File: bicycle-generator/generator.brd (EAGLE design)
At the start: 100 x 80 mm, 61 parts, among them IC1 MC34063AD, K1 ARK500/2, K2 ARK500/2, K3 ARK500/2, K4 ARK500/2, K5 ARK500/2, K6 HEAT_NPN, K7 ARK500/2, K8 ARK500/2, Q1 IRF3704S, Q4 IRFR5305, T1 BC807, T2 BC807, X1 CV_LED, X2 PWR_LED, X3 5V_SW, X4 5V_LED, X5 5V_OUT

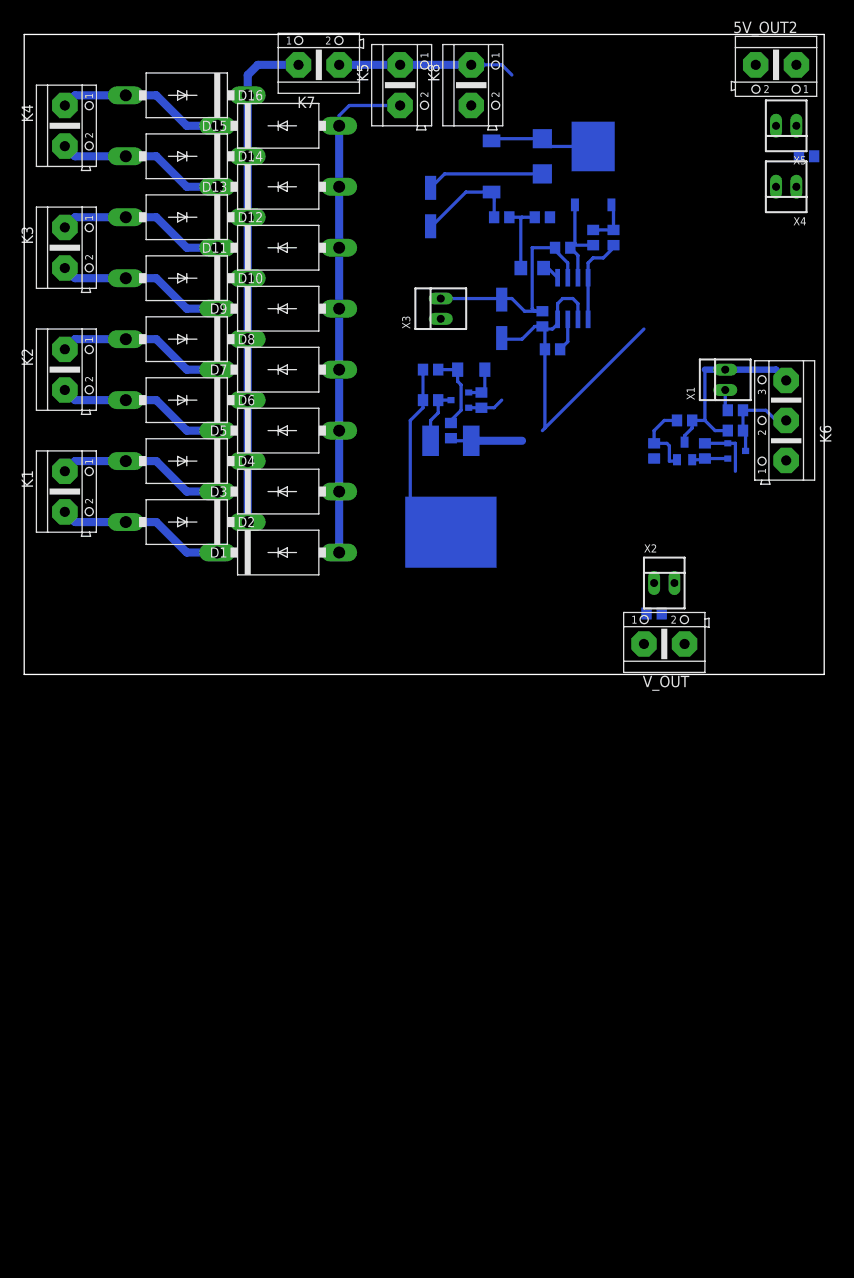
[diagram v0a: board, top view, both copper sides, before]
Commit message: Use N-channel MOSFET with pulldown.
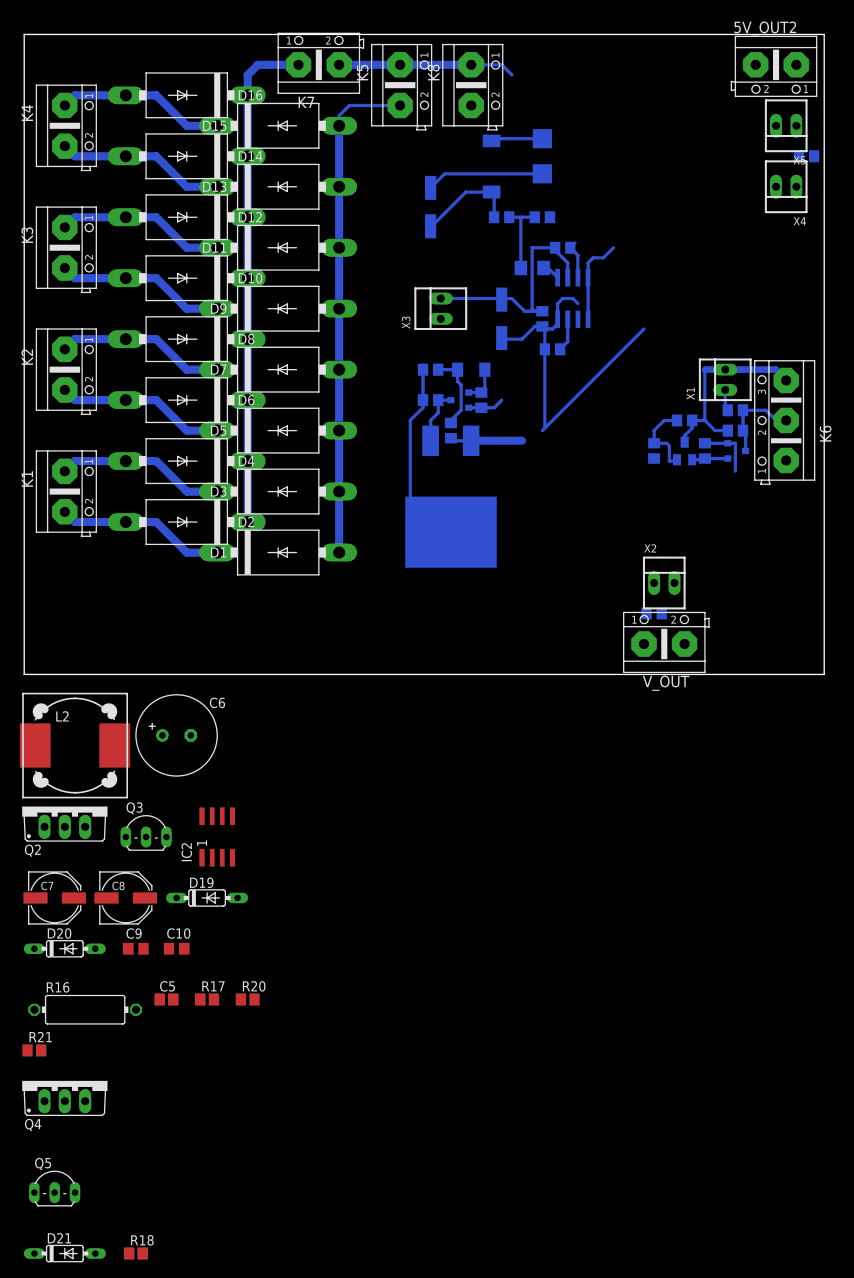
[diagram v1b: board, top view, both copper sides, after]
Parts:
- removed R19: 330, rcl:R0805
- added C10: 10n, rcl:C0805
- added C5: 680p, resistor:C0805
- added C6: 10uF, 200V, resistor:E3,5-10
- added C7, C8: 100uF, resistor:PANASONIC_D
- added C9: 100n, rcl:C0805
- added D19: BAV21, diode:DO35-7
- added D20, D21: 1N914, diode:DO35-7
- added IC2: MC34063SO, #Krakonos:SOP08
- added L2: DR127, 330uH, inductors:DR127
- added Q2: IRF740, transistor-power:TO220BV
- added Q3, Q5: MPSA56, transistor-pnp:TO92-CBE
- added R16: R1, 2W, resistor:V234/12
- added R17, R21: 1k, resistor:R0805
- added R20: 150k, 200V, resistor:R0805
- Q4: value IRFR5305 -> IRF740; device transistor-power:D-PAK_TO252AA -> transistor-power:TO220BV
- R18: value 820 -> 1k; device rcl:R0805 -> resistor:R0805
- moved R18 140.3 mm to (14.0, -72.4), flipped to the top, turned to 0 degrees
- moved Q4 132.0 mm to (5.08, -50.8), flipped to the top
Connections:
- new net 200V: C6.+, D19.C, R20.1
- new net N$25: C10.1, IC2.5, R17.2, R20.2
- new net N$26: C5.1, IC2.3
- new net N$29: D19.A, L2.2, Q2.D
- new net N$30: D20.C, Q2.G, Q3.E
- new net N$31: D20.A, IC2.2, Q3.B, R21.1
- new net N$32: C8.+, IC2.1, IC2.7, IC2.8, L2.1, R16.2
- new net N$33: D21.A, IC1.2
- new net VCC: C7.+, C9.1, IC2.6, R16.1
- net GND: now also C10.2, C5.2, C6.-, C7.-, C8.-, C9.2, IC2.4, Q2.S, Q3.C, Q5.C, R17.1, R18.2, R21.2; no longer IC1.2
- net N$15: now also D21.C, Q4.G, Q5.E; no longer IC1.1, IC1.8, R18.2
- net N$19: now also Q4.S; no longer Q4.4
- net N$27: now also IC1.1, IC1.7, IC1.8, Q4.D, R13.2; no longer Q4.1, R18.1, R19.2
- net N$28: now also Q5.B, R18.1; no longer IC1.7, Q4.3, R13.2, R19.1
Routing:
- net N$28: track 12.7 -> 0.00 mm
- net N$15: track 11.3 -> 0.00 mm
- net N$27: track 5.79 -> 16.4 mm
- net N$19: track 13.2 -> 7.83 mm
- net GND: track 69.7 -> 67.8 mm

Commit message: First version routed.
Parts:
- removed C10: 10n, rcl:C0805
- removed C5: 680p, resistor:C0805
- removed C6: 10uF, 200V, resistor:E3,5-10
- removed C7, C8: 100uF, resistor:PANASONIC_D
- removed C9: 100n, rcl:C0805
- removed D20, D21: 1N914, diode:DO35-7
- removed IC2: MC34063SO, #Krakonos:SOP08
- removed L2: DR127, 330uH, inductors:DR127
- removed Q3, Q5: MPSA56, transistor-pnp:TO92-CBE
- removed Q4: IRF740, transistor-power:TO220BV
- removed R16: R1, 2W, resistor:V234/12
- removed R17, R21: 1k, resistor:R0805
- removed R20: 150k, 200V, resistor:R0805
- added T3: (no value), transistor:SOT23-BEC
- D19: value BAV21 -> LL4148-MINIMELF; device diode:DO35-7 -> diode:SOD80C
- Q2: value IRF740 -> IRF3704S; device transistor-power:TO220BV -> transistor-power:D2PACK
- moved R18 114.8 mm to (62.2, 31.8), flipped to the bottom, turned to 90 degrees
- moved D19 66.9 mm to (59.7, 27.9), flipped to the bottom, turned to 180 degrees
- moved Q2 65.4 mm to (62.2, 15.2), flipped to the bottom, turned to 180 degrees
- moved C3 56.3 mm to (77.5, 8.89), turned to 180 degrees
- moved R14 51.5 mm to (83.8, 15.2), turned to 90 degrees
- moved X4 50.6 mm to (85.1, 11.4), turned to 0 degrees
- moved K6 50.1 mm to (69.8, 74.9), turned to 180 degrees
- moved V_OUT 48.9 mm to (87.6, 52.1), turned to 270 degrees
- moved X5 48.1 mm to (85.1, 21.6), turned to 0 degrees
- moved L1 47.9 mm to (76.2, 19.1), turned to 270 degrees
- moved R11 47.7 mm to (80.0, 14.0), turned to 180 degrees
- moved 5V_OUT2 46.4 mm to (86.4, 30.5), turned to 270 degrees
- moved R12 44.4 mm to (74.9, 14.0), turned to 180 degrees
- moved D18 43.5 mm to (69.8, 21.6)
- moved T2 43.4 mm to (73.7, 68.6), turned to 0 degrees
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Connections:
- removed net 200V: C6.+, D19.C, R20.1
- removed net N$25: C10.1, IC2.5, R17.2, R20.2
- removed net N$26: C5.1, IC2.3
- removed net N$29: D19.A, L2.2, Q2.D
- removed net N$30: D20.C, Q2.G, Q3.E
- removed net N$31: D20.A, IC2.2, Q3.B, R21.1
- removed net N$32: C8.+, IC2.1, IC2.7, IC2.8, L2.1, R16.2
- removed net N$33: D21.A, IC1.2
- removed net VCC: C7.+, C9.1, IC2.6, R16.1
- net GND: now also T3.C; no longer C10.2, C5.2, C6.-, C7.-, C8.-, C9.2, IC2.4, Q2.S, Q3.C, Q5.C, R17.1, R21.2
- net N$15: now also D19.C, Q2.1, T3.E; no longer D21.C, Q4.G, Q5.E
- net N$19: now also Q2.3; no longer Q4.S
- net N$27: now also Q2.2; no longer Q4.D
- net N$28: now also D19.A, IC1.2, T3.B; no longer Q5.B
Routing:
- net GND: track 67.8 -> 174.5 mm
- net V+: track 33.9 -> 110.6 mm
- net V-: track 112.7 -> 139.7 mm
- net +5V: track 13.1 -> 35.2 mm
- net N$27: track 16.4 -> 38.4 mm
- net N$28: track 0.00 -> 12.1 mm
- net N$21: track 2.25 -> 11.4 mm
- net N$15: track 0.00 -> 7.53 mm
- net N$19: track 7.83 -> 13.5 mm
- net N$23: track 0.00 -> 3.20 mm
- net N$11: track 9.59 -> 12.7 mm
- net N$22: track 0.00 -> 2.86 mm
- net N$24: track 29.8 -> 32.4 mm
- net N$16: track 4.15 -> 2.61 mm

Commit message: Routed board.
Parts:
- L1: device rcl:PIS2816 -> rcl:TJ3-U1
- moved X2 20.5 mm to (86.4, 57.1), turned to 270 degrees
- moved R10 19.2 mm to (82.5, 61.0), turned to 0 degrees
- moved V_OUT 15.3 mm to (86.4, 67.3)
- moved R11 14.2 mm to (77.5, 27.9), turned to 270 degrees
- moved R12 14.0 mm to (74.9, 27.9), turned to 90 degrees
- moved C3 12.8 mm to (76.2, 21.6)
- moved X3 11.5 mm to (86.4, 50.8)
- moved C1 9.55 mm to (65.4, 40.0)
- moved IC1 8.89 mm to (71.1, 38.1)
- moved L1 8.89 mm to (76.2, 27.9), turned to 180 degrees
- moved R13 8.89 mm to (77.5, 38.1)
- moved X4 8.89 mm to (85.1, 20.3)
- moved X5 8.89 mm to (85.1, 30.5)
- moved Q2 8.89 mm to (62.2, 24.1)
- moved R14 8.89 mm to (83.8, 24.1)
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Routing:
- net V-: track 139.7 -> 131.1 mm
- net N$11: track 12.7 -> 5.51 mm
- net N$27: track 38.4 -> 42.5 mm
- net N$3: track 4.60 -> 7.98 mm
- net V+: track 110.6 -> 107.5 mm
- net N$12: track 9.94 -> 6.88 mm
- net N$24: track 32.4 -> 30.0 mm
- net GND: track 174.5 -> 172.3 mm
- net N$19: track 13.5 -> 11.4 mm
- net N$28: track 12.1 -> 13.9 mm
- net N$23: track 3.20 -> 4.66 mm
- net N$15: track 7.53 -> 8.91 mm
- net +5V: track 35.2 -> 33.9 mm
- net N$16: track 2.61 -> 3.25 mm
- net N$7: track 11.1 -> 10.5 mm
- added copper zone on layer 16, net GND
- added copper zone on layer 16, net N$20
- added copper zone on layer 16, net N$25
- added copper zone on layer 16, net V-
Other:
- board size 100 x 80 mm -> 93.7 x 69.8 mm

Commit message: Values of parts.
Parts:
- C1: value 220p -> 680p
- D17: value (none) -> 6V2
- R1, R3, R8: value (none) -> 10k
- R10, R2, R6, R7, R9: value (none) -> 1k
- R14: value (none) -> 330
- R15: value 3k -> 0R
- R4: value (none) -> 56k
- R5: value (none) -> 15k

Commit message: Commit before merge
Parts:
- moved K1 83.5 mm to (88.6, 22.9), flipped to the bottom
- moved K2 83.5 mm to (88.6, 38.1), flipped to the bottom
- moved K3 83.5 mm to (88.6, 53.3), flipped to the bottom
- moved K4 83.5 mm to (88.6, 68.6), flipped to the bottom
- moved 5V_OUT2 79.1 mm to (7.29, 39.4), flipped to the bottom
- moved V_OUT 79.1 mm to (7.29, 67.3), flipped to the bottom
- moved X2 79.1 mm to (7.29, 57.1), flipped to the bottom
- moved X3 79.1 mm to (7.29, 50.8), flipped to the top
- moved X4 76.5 mm to (8.56, 20.3), flipped to the bottom
- moved X5 76.5 mm to (8.56, 30.5), flipped to the bottom
- moved R14 74.0 mm to (9.83, 24.1), flipped to the top
- moved R10 71.5 mm to (11.1, 61.0), flipped to the top
- moved D17 61.3 mm to (16.2, 53.3), flipped to the top
- moved R11 61.3 mm to (16.2, 27.9), flipped to the top
- moved R13 61.3 mm to (16.2, 38.1), flipped to the top
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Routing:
- added copper zone on layer 1, net GND
- added copper zone on layer 1, net N$20
- added copper zone on layer 1, net N$25
- added copper zone on layer 1, net V-
- removed copper zone on layer 16, net GND
- removed copper zone on layer 16, net N$20
- removed copper zone on layer 16, net N$25
- removed copper zone on layer 16, net V-
